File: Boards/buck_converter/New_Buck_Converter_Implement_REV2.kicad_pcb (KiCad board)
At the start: 2 copper layers, 20 parts, among them J101 Conn_01x02_Female, J102 Conn_01x02_Female, U101 TPS560430YF

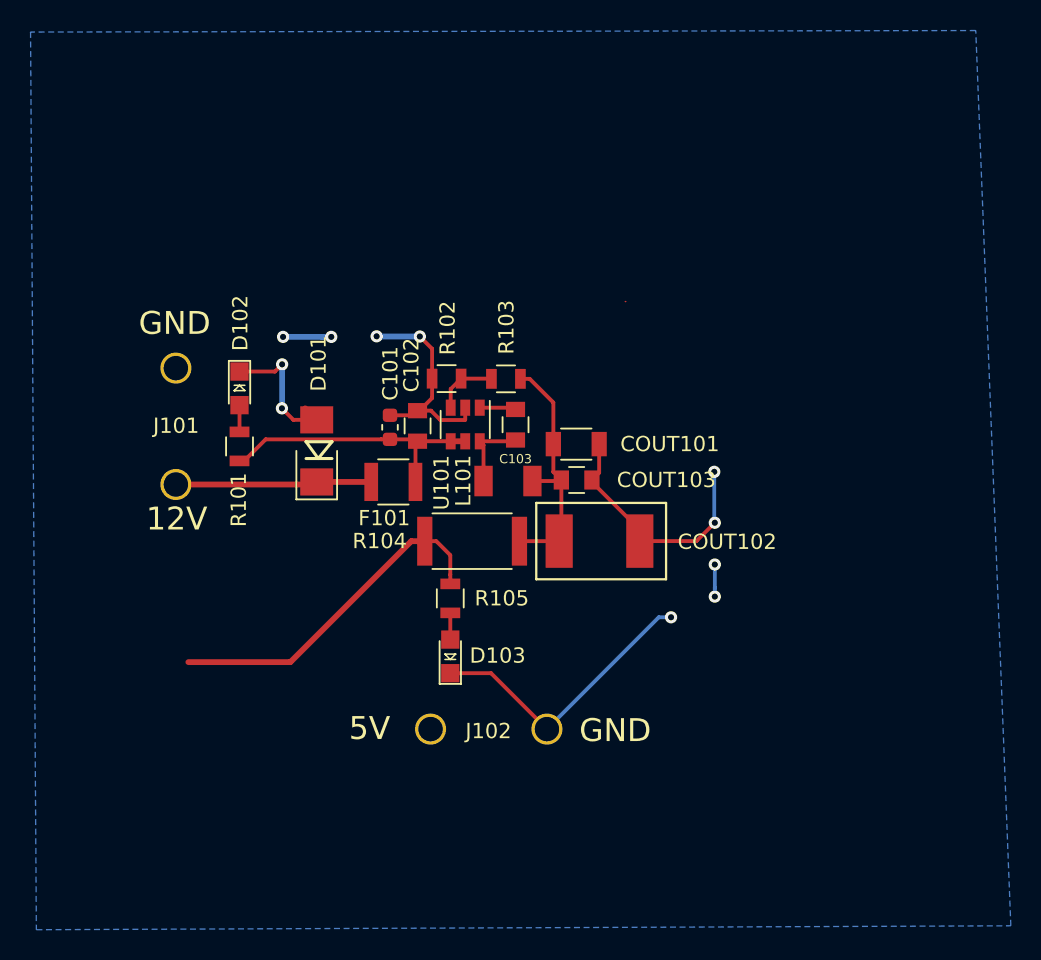
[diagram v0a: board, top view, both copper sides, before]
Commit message: Updated the buck converter footprint for implementation
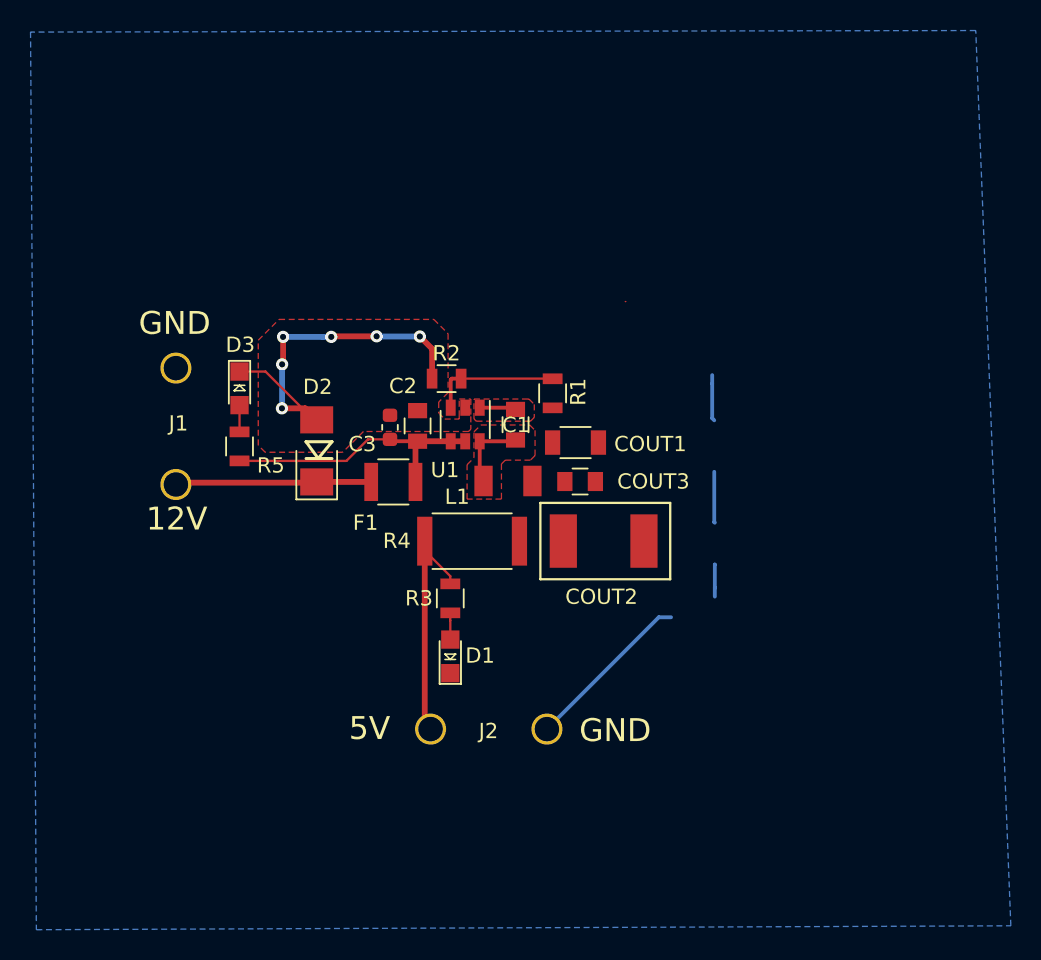
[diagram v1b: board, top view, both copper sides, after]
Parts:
- removed L101: L_100uH, footprints:L_100uH
- added L1: L_100uH, footprints:L_100uH, F.Cu at (129.5, 105.7)
- C2: renamed from C102; value C_2.2uF -> C_0.1uF
- C3: renamed from C101; value C_0.1uF -> C_2.2uF
- moved R1 3.20 mm to (132.4, 99.9), turned to 90 degrees
- moved COUT2 0.27 mm to (133.1, 109.6)
- moved COUT3 0.25 mm to (134.2, 105.7)
- moved COUT1 0.11 mm to (133.9, 103.2)
- renumbered C103 to C1, COUT101 to COUT1, COUT102 to COUT2, COUT103 to COUT3, D103 to D1, D101 to D2, D102 to D3, F101 to F1, J101 to J1, J102 to J2, R103 to R1, R102 to R2, R105 to R3, R104 to R4, R101 to R5, U101 to U1
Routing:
- net VCC: track 22.7 -> 2.27 mm
- net GND: track 65.5 -> 45.4 mm, vias 11 -> 6
- net Net-(COUT1-Pad1): track 17.3 -> 0.01 mm
- net /5V: track 0.55 -> 12.5 mm
- net Net-(R1-Pad2): track 4.18 -> 8.53 mm
- added copper zone on F.Cu, net Net-(C1-Pad1)
- added copper zone on F.Cu, net Net-(C1-Pad2)
